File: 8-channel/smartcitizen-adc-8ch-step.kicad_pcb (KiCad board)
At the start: 2 copper layers, 42.4 x 44.2 mm, 46 parts, among them J1 GROVE1, J2 GROVE2, J5 Conn_02x05_Odd_Even, M1 PINHD-1x06-HEADER, M2 PINHD-1x06-HEADER, M3 PINHD-1x06-HEADER, M4 PINHD-1x06-HEADER, T1 NMOSFETSOT23, T2 NMOSFETSOT23, U1 ADS1115IDGSR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

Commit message: 8-channel board changes and schematic
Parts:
- C10: value 100nF -> 330nF
- R10, R11: footprint Resistor_SMD:R_01005_0402Metric -> Resistor_SMD:R_0402_1005Metric
- U5: value LM3480-5.0 -> PJ78605SA
- moved LO2 6.77 mm to (174.6, 99.5), turned to 270 degrees
- turned LO1 to 270 degrees
- turned OSH1 to 90 degrees
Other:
- board text added: "10/01/2022"
- board text removed: "11/07/2021"

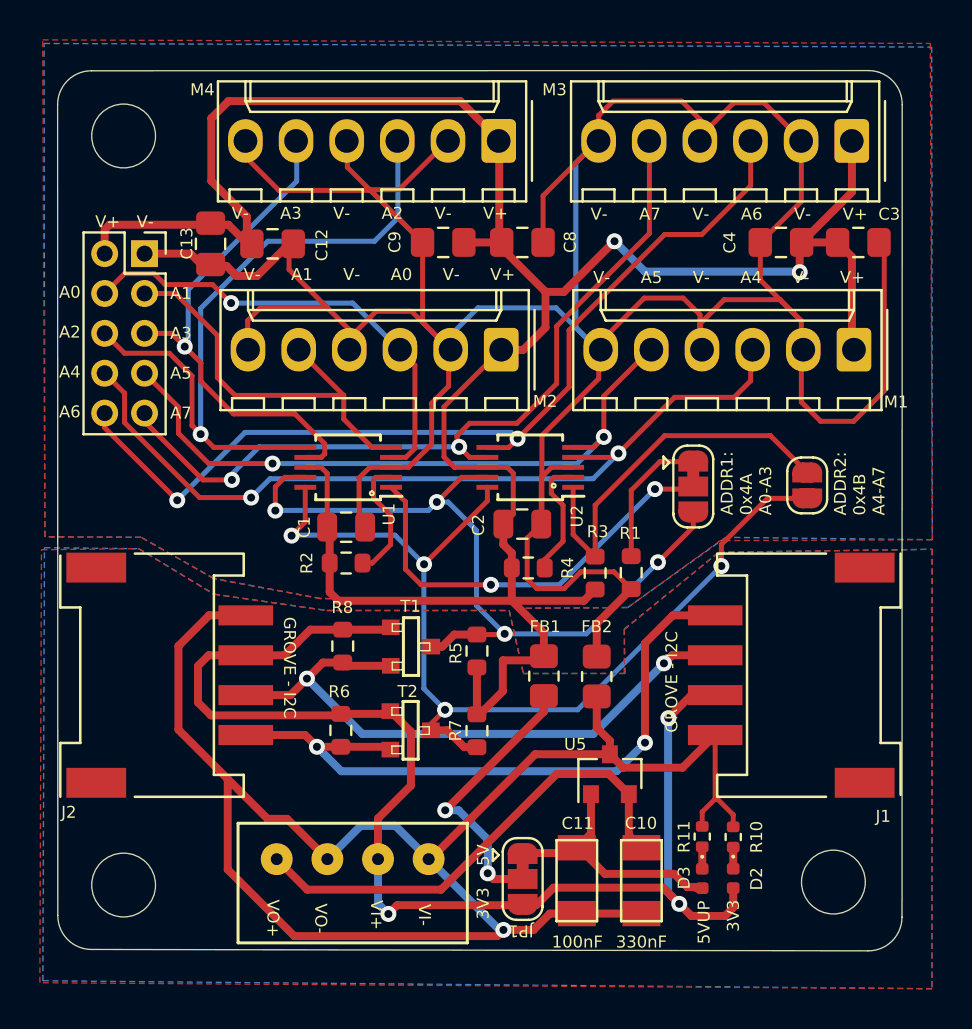
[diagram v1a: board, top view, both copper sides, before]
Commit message: Fix missing symbols
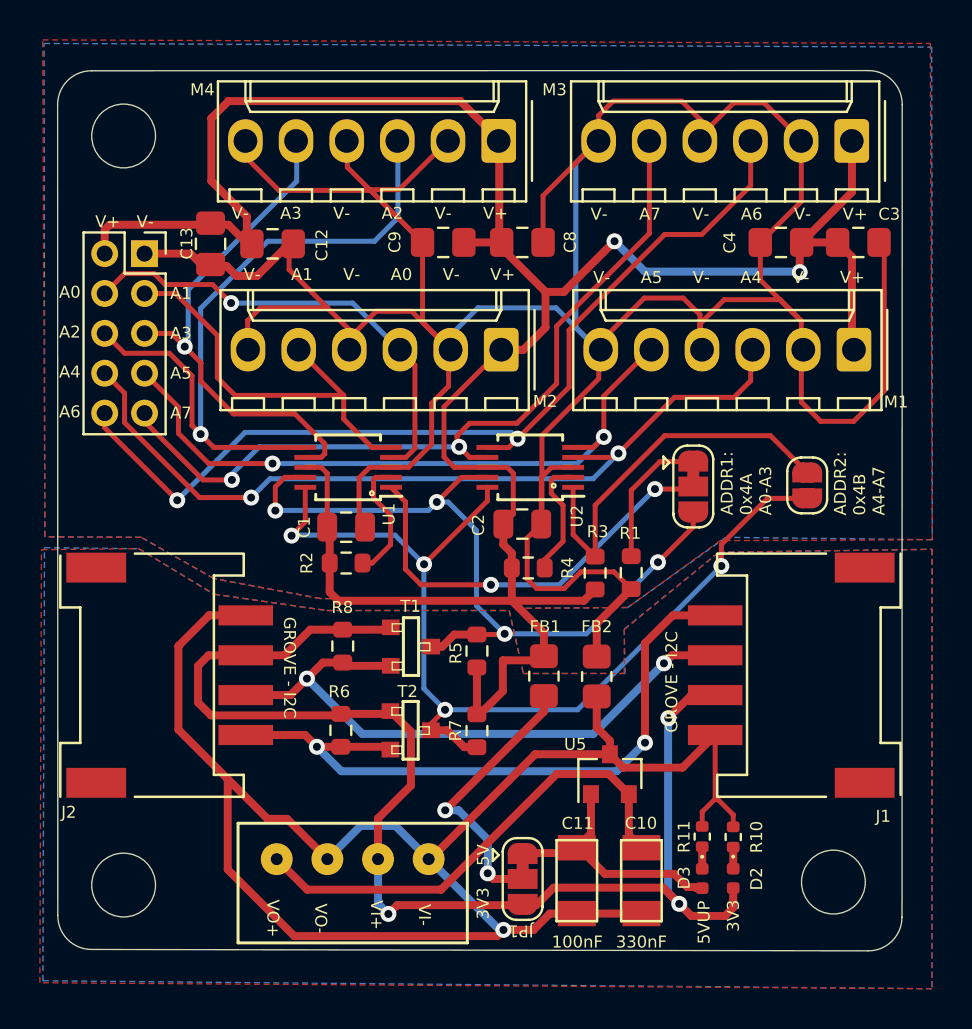
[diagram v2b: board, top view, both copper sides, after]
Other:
- board size 42.4 x 44.2 mm -> 42.4 x 44.1 mm
- net class Default removed
- net class Non-ADS removed
